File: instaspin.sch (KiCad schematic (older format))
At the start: 58 parts, among them J1 CONN_01X02, J14 CONN_01X05, J15 CONN_01X03, J2 CONN_01X08, J3 CONN_02X05, U1 ACPL-M61L, U2 TMS320F28069M, U3 ADM3053, Y1 CSTCE20M0V13C

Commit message: Placement almost complete
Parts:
- removed W22: TEST_1P, Measurement_Points:Measurement_Point_Round-SMD-Pad_Small, symbol TEST_1P
- W13, W14, W15, W17, W19, W20: footprint Measurement_Points:Measurement_Point_Round-SMD-Pad_Small -> Measurement_Points:Measurement_Point_Round-TH_Small
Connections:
- net LED1: now also D1.1 (K); no longer D1.2 (K)
- net SW_BRAKE: now also D3.2 (K); no longer D3.1 (K)
- net SW_EMERG: now also D3.1 (K); no longer D3.2 (K)
- net at J2.5 (P5), R4.1: now also D1.2 (K); no longer D1.1 (K)
- net VDD_MON: now reaches R7.2, R8.1, U2.26 (ADCIN_B5)
- net at W19.1: now also U2.75 (GPIO13/~TZ2~/SPISOMIB); no longer U2.31 (GPIO25/ECAP2/SPISOMIB)
- net at W20.1: now also U2.76 (GPIO14/~TZ3~/SCITXDB/SPICLKB); no longer U2.62 (*GPIO26/ECAP3/SPICLKB/USB0DP)
- net VREFHI: now reaches C21.1, R5.2, R6.1, U2.19 (ADCIN_A0/VREFHI)
- no-connect marks 10 -> 11
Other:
- moved on the sheet: W19, W20
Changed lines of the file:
@@
 F 0 "W17" V 6200 4400 50  0000 C CNN
 F 1 "TEST_1P" V 6304 4224 50  0001 C CNN
-F 2 "Measurement_Points:Measurement_Point_Round-SMD-Pad_Small" H 6400 4150 50  0001 C CNN
+F 2 "Measurement_Points:Measurement_Point_Round-TH_Small" H 6400 4150 50  0001 C CNN
 F 3 "" H 6400 4150 50  0000 C CNN
 	1    6200 4150
@@
 L TEST_1P W19
 U 1 1 57F638C1
-P 6200 4250
-F 0 "W19" V 6200 4500 50  0000 C CNN
-F 1 "TEST_1P" V 6304 4324 50  0001 C CNN
-F 2 "Measurement_Points:Measurement_Point_Round-SMD-Pad_Small" H 6400 4250 50  0001 C CNN
-F 3 "" H 6400 4250 50  0000 C CNN
-	1    6200 4250
+P 6200 3050
+F 0 "W19" V 6200 3300 50  0000 C CNN
+F 1 "TEST_1P" V 6304 3124 50  0001 C CNN
+F 2 "Measurement_Points:Measurement_Point_Round-TH_Small" H 6400 3050 50  0001 C CNN
+F 3 "" H 6400 3050 50  0000 C CNN
+	1    6200 3050
 	0    1    1    0
 $EndComp
@@
 L TEST_1P W20
 U 1 1 57F63968
-P 6200 4350
-F 0 "W20" V 6200 4600 50  0000 C CNN
-F 1 "TEST_1P" V 6304 4424 50  0001 C CNN
-F 2 "Measurement_Points:Measurement_Point_Round-SMD-Pad_Small" H 6400 4350 50  0001 C CNN
-F 3 "" H 6400 4350 50  0000 C CNN
-	1    6200 4350
-	0    1    1    0
-$EndComp
-$Comp
-L TEST_1P W22
-U 1 1 57F63A0E
-P 6200 4450
-F 0 "W22" V 6200 4700 50  0000 C CNN
-F 1 "TEST_1P" V 6304 4524 50  0001 C CNN
-F 2 "Measurement_Points:Measurement_Point_Round-SMD-Pad_Small" H 6400 4450 50  0001 C CNN
-F 3 "" H 6400 4450 50  0000 C CNN
-	1    6200 4450
+P 6200 3150
+F 0 "W20" V 6200 3400 50  0000 C CNN
+F 1 "TEST_1P" V 6304 3224 50  0001 C CNN
+F 2 "Measurement_Points:Measurement_Point_Round-TH_Small" H 6400 3150 50  0001 C CNN
+F 3 "" H 6400 3150 50  0000 C CNN
+	1    6200 3150
 	0    1    1    0
 $EndComp
@@
 F 0 "W15" V 6200 4300 50  0000 C CNN
 F 1 "TEST_1P" V 6304 4124 50  0001 C CNN
-F 2 "Measurement_Points:Measurement_Point_Round-SMD-Pad_Small" H 6400 4050 50  0001 C CNN
+F 2 "Measurement_Points:Measurement_Point_Round-TH_Small" H 6400 4050 50  0001 C CNN
 F 3 "" H 6400 4050 50  0000 C CNN
 	1    6200 4050
@@
 F 0 "W13" V 6200 3800 50  0000 C CNN
 F 1 "TEST_1P" V 6304 3624 50  0001 C CNN
-F 2 "Measurement_Points:Measurement_Point_Round-SMD-Pad_Small" H 6400 3550 50  0001 C CNN
+F 2 "Measurement_Points:Measurement_Point_Round-TH_Small" H 6400 3550 50  0001 C CNN
 F 3 "" H 6400 3550 50  0000 C CNN
 	1    6200 3550
@@
 F 0 "W14" V 6200 3900 50  0000 C CNN
 F 1 "TEST_1P" V 6304 3724 50  0001 C CNN
-F 2 "Measurement_Points:Measurement_Point_Round-SMD-Pad_Small" H 6400 3650 50  0001 C CNN
+F 2 "Measurement_Points:Measurement_Point_Round-TH_Small" H 6400 3650 50  0001 C CNN
 F 3 "" H 6400 3650 50  0000 C CNN
 	1    6200 3650
@@
 NoConn ~ 6200 2750
 NoConn ~ 6200 2950
-NoConn ~ 6200 3050
-NoConn ~ 6200 3150
 NoConn ~ 6200 3250
 NoConn ~ 6200 3350
@@
 F 3 "" H 9900 3600 50  0000 C CNN
 	1    9900 3600
-	1    0    0    -1
+	-1   0    0    -1
 $EndComp
 $Comp
@@
 F 3 "" H 9650 3000 50  0000 C CNN
 	1    9650 3000
-	0    -1   -1   0
+	0    -1   1    0
 $EndComp
 $Comp
@@
 	1    0    0    -1
 $EndComp
+NoConn ~ 6200 4250
+NoConn ~ 6200 4350
+NoConn ~ 6200 4450
+Text Label 2450 4350 0    60   ~ 0
+VREFHI
+Text Label 1250 4800 0    60   ~ 0
+VDD_MON
 $EndSCHEMATC

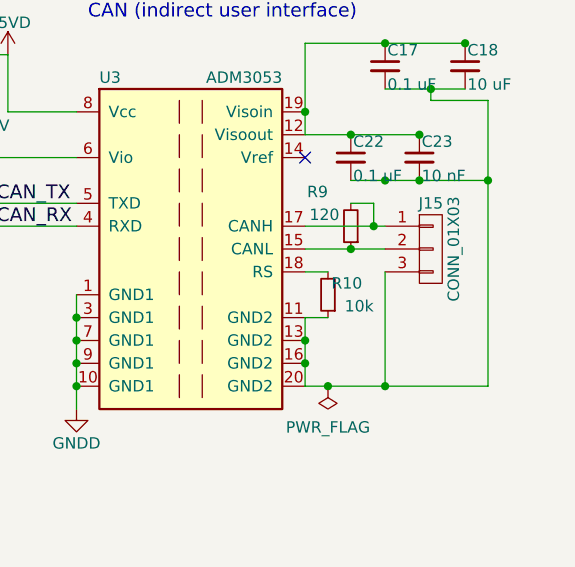
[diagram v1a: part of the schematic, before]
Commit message: Placed AGND plane
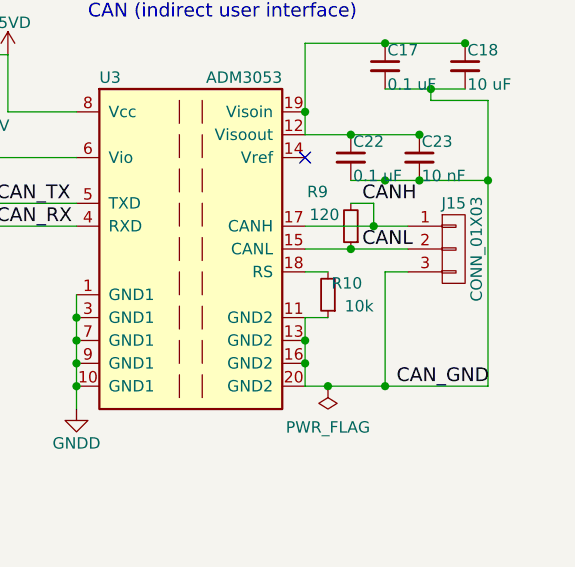
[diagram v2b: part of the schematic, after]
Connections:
- net CAN_GND: now reaches C17.2, C18.2, C22.2, C23.2, J15.3 (P3), R10.1, U3.11 (GND2), U3.13 (GND2), U3.16 (GND2), U3.20 (GND2)
- net CANL: now reaches J15.2 (P2), R9.1, U3.15 (CANL)
- net CANH: now reaches J15.1 (P1), R9.2, U3.17 (CANH)
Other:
- moved on the sheet: J15
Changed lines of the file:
@@
-$EndComp
-$Comp
-L CONN_01X03 J15
-U 1 1 57F682F4
-P 9750 5150
-F 0 "J15" H 9750 5350 50  0000 C CNN
-F 1 "CONN_01X03" V 9850 5150 50  0000 C CNN
-F 2 "Connectors_Molex:Molex_PicoBlade_53261-0371" H 9750 5150 50  0001 C CNN
-F 3 "" H 9750 5150 50  0000 C CNN
-	1    9750 5150
-	1    0    0    -1
 $EndComp
 $Comp
@@
 	9200 5250 9300 5250
 Wire Wire Line
-	9200 5050 9550 5050
-Wire Wire Line
-	9200 5150 9550 5150
-Wire Wire Line
-	9550 5750 9550 5250
+	9200 5050 9650 5050
+Wire Wire Line
+	9200 5150 9650 5150
 Wire Wire Line
 	9200 5750 10000 5750
@@
 Text Label 1250 4800 0    60   ~ 0
 VDD_MON
+Text Label 9600 5750 0    60   ~ 0
+CAN_GND
+Text Label 9450 4950 0    60   ~ 0
+CANH
+Text Label 9450 5150 0    60   ~ 0
+CANL
+Wire Wire Line
+	9650 5250 9550 5250
+Wire Wire Line
+	9550 5250 9550 5750
+$Comp
+L CONN_01X03 J15
+U 1 1 57F682F4
+P 9850 5150
+F 0 "J15" H 9850 5350 50  0000 C CNN
+F 1 "CONN_01X03" V 9950 5150 50  0000 C CNN
+F 2 "Connectors_Molex:Molex_PicoBlade_53261-0371" H 9850 5150 50  0001 C CNN
+F 3 "" H 9850 5150 50  0000 C CNN
+	1    9850 5150
+	1    0    0    -1
+$EndComp
 $EndSCHEMATC

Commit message: Route CAN isolated section
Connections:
- net CAN_GND: now also J15.1 (P1); no longer J15.3 (P3)
- net CANH renamed CAN+
- net CAN+: now also J15.3 (P3); no longer J15.1 (P1)
- net CANL renamed CAN-
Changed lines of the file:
@@
 CAN_GND
 Text Label 9450 4950 0    60   ~ 0
-CANH
+CAN+
 Text Label 9450 5150 0    60   ~ 0
-CANL
+CAN-
 Wire Wire Line
 	9650 5250 9550 5250
@@
 F 3 "" H 9850 5150 50  0000 C CNN
 	1    9850 5150
-	1    0    0    -1
+	1    0    0    1
 $EndComp
 $EndSCHEMATC

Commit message: 3.3V and 1.8V supplies routed; fixed wrong connections on 1.8V regulator
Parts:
- added W4: TEST_1P, Measurement_Points:Measurement_Point_Round-TH_Small, symbol TEST_1P
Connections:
- net TEMP_EN: now also U2.61 (*GPIO27/HRCAP2/~SPISTEB~/USB0DM); no longer U2.80 (GPIO33/SCLA/EPWMSYNCO/~ADCSOCBO)
- net ~DSP_RESET: now also W4.1
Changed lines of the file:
@@
 Text HLabel 6200 2850 2    60   Input ~ 0
 TEMP_PWM
-Text HLabel 6200 5050 2    60   Output ~ 0
+Text HLabel 6200 4450 2    60   Output ~ 0
 TEMP_EN
 Text HLabel 6200 1750 2    60   Output ~ 0
@@
 NoConn ~ 6200 4250
 NoConn ~ 6200 4350
-NoConn ~ 6200 4450
+NoConn ~ 6200 5050
 Text Label 2450 4350 0    60   ~ 0
 VREFHI
@@
 	1    0    0    1
 $EndComp
+$Comp
+L TEST_1P W4
+U 1 1 58072EEC
+P 1450 2550
+F 0 "W4" V 1450 2800 50  0000 C CNN
+F 1 "TEST_1P" V 1554 2624 50  0001 C CNN
+F 2 "Measurement_Points:Measurement_Point_Round-TH_Small" H 1650 2550 50  0001 C CNN
+F 3 "" H 1650 2550 50  0000 C CNN
+	1    1450 2550
+	1    0    0    -1
+$EndComp
+Connection ~ 1450 2550
 $EndSCHEMATC

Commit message: Silkscreen done both sides, added aux LED
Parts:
- added D34: LED, LEDs:LED_0603, symbol LED
- added R51: 330, Resistors_SMD:R_0402, symbol R_Small
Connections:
- net +3V3: now also R51.1
- net at U2.31 (GPIO25/ECAP2/SPISOMIB): now also D34.1 (K)
- new net: D34.2 (A), R51.2
- no-connect marks 11 -> 10

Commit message: V2.1: Fixes for V2.0 bugs
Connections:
- net PWR_RDY renamed ~PWR_RDY
- net ~FLT_DESAT renamed FLT_DESAT
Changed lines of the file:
@@
 PWM_AL
 Text HLabel 6200 4550 2    60   Input ~ 0
-~FLT_DESAT
+FLT_DESAT
 Text HLabel 6200 5250 2    60   Input ~ 0
-PWR_RDY
+~PWR_RDY
 Text HLabel 6200 4950 2    60   Output ~ 0
 ~PWR_RESET

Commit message: errata updates and schematic comments
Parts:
- D34: symbol LED -> LED-RESCUE-sictroller
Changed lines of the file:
@@
 EESchema Schematic File Version 2
+LIBS:sictroller-rescue
 LIBS:power
 LIBS:device
@@
 $EndComp
 $Comp
-L LED D34
+L LED-RESCUE-sictroller D34
 U 1 1 580C54AB
 P 7050 4050
+AR Path="/580C54AB" Ref="D34"  Part="1"
+AR Path="/57A162B5/580C54AB" Ref="D34"  Part="1"
 F 0 "D34" H 7050 4150 50  0000 C CNN
 F 1 "LED" H 7050 3950 50  0000 C CNN
